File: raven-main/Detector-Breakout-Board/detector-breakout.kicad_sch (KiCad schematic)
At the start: 0 parts

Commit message: Added a power connector
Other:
- added sheet detector (detector.kicad_sch)
- added sheet power (power.kicad_sch)
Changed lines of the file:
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@@
 	(generator_version "10.0")
 	(paper "A4")
+	(sheet
+		(at 41.91 34.29)
+		(size 13.97 16.51)
+		(exclude_from_sim no)
+		(in_bom yes)
+		(on_board yes)
+		(dnp no)
+		(fields_autoplaced yes)
+		(stroke
+			(width 0.1524)
+			(type solid)
+		)
+		(fill
+			(color 0 0 0 0)
+		)
+		(property "Sheetname" "power"
+			(at 41.91 33.5784 0)
+			(show_name no)
+			(do_not_autoplace no)
+			(effects
+				(font
+					(size 1.27 1.27)
+				)
+				(justify left bottom)
+			)
+		)
+		(property "Sheetfile" "power.kicad_sch"
+			(at 41.91 51.3846 0)
+			(show_name no)
+			(do_not_autoplace no)
+			(effects
+				(font
+					(size 1.27 1.27)
+				)
+				(justify left top)
+			)
+		)
+		(instances
+			(project "detector-breakout"
+				(path "/88625785-cc97-4732-ad3f-8e674b21ece1"
+					(page "2")
+				)
+			)
+		)
+	)
+	(sheet
+		(at 77.47 34.29)
+		(size 15.24 16.51)
+		(exclude_from_sim no)
+		(in_bom yes)
+		(on_board yes)
+		(dnp no)
+		(fields_autoplaced yes)
+		(stroke
+			(width 0.1524)
+			(type solid)
+		)
+		(fill
+			(color 0 0 0 0)
+		)
+		(property "Sheetname" "detector"
+			(at 77.47 33.5784 0)
+			(show_name no)
+			(do_not_autoplace no)
+			(effects
+				(font
+					(size 1.27 1.27)
+				)
+				(justify left bottom)
+			)
+		)
+		(property "Sheetfile" "detector.kicad_sch"
+			(at 77.47 51.3846 0)
+			(show_name no)
+			(do_not_autoplace no)
+			(effects
+				(font
+					(size 1.27 1.27)
+				)
+				(justify left top)
+			)
+		)
+		(pin "Detector_Out_A" output
+			(at 92.71 36.83 0)
+			(effects
+				(font
+					(size 1.27 1.27)
+				)
+				(justify right)
+			)
+		)
+		(pin "Detector_Out_B" input
+			(at 92.71 39.37 0)
+			(effects
+				(font
+					(size 1.27 1.27)
+				)
+				(justify right)
+			)
+		)
+		(instances
+			(project "detector-breakout"
+				(path "/88625785-cc97-4732-ad3f-8e674b21ece1"
+					(page "3")
+				)
+			)
+		)
+	)
 	(sheet_instances
 		(path "/"

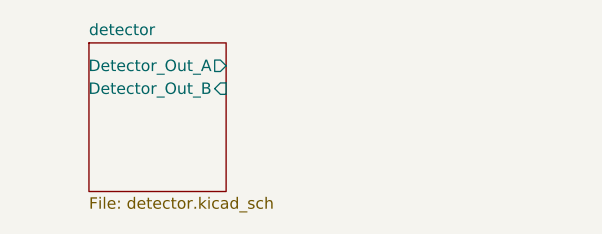
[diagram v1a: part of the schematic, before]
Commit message: Added power and output pins
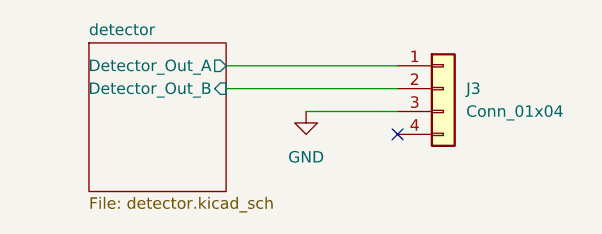
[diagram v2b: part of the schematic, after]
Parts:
- added J3: Conn_01x04, Connector_PinHeader_2.54mm:PinHeader_1x04_P2.54mm_Vertical, symbol Connector_Generic:Conn_01x04
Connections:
- net detector/Detector_Out_A: now also J3.1 (Pin_1)
- net detector/Detector_Out_B: now also J3.2 (Pin_2)
- new net GND: J3.3 (Pin_3)
- no-connect marks 0 -> 1
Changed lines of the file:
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@@
 	(generator_version "10.0")
 	(paper "A4")
+	(no_connect
+		(at 111.76 44.45)
+	)
+	(wire
+		(pts
+			(xy 92.71 39.37) (xy 111.76 39.37)
+		)
+		(stroke
+			(width 0)
+			(type default)
+		)
+	)
+	(wire
+		(pts
+			(xy 101.6 41.91) (xy 111.76 41.91)
+		)
+		(stroke
+			(width 0)
+			(type default)
+		)
+	)
+	(wire
+		(pts
+			(xy 92.71 36.83) (xy 111.76 36.83)
+		)
+		(stroke
+			(width 0)
+			(type default)
+		)
+	)
+	(symbol
+		(lib_id "power:GND")
+		(at 101.6 41.91 0)
+		(unit 1)
+		(body_style 1)
+		(exclude_from_sim no)
+		(in_bom yes)
+		(on_board yes)
+		(in_pos_files yes)
+		(dnp no)
+		(fields_autoplaced yes)
+		(property "Reference" "#PWR03"
+			(at 101.6 48.26 0)
+			(hide yes)
+			(show_name no)
+			(do_not_autoplace no)
+			(effects
+				(font
+					(size 1.27 1.27)
+				)
+			)
+		)
+		(property "Value" "GND"
+			(at 101.6 46.99 0)
+			(show_name no)
+			(do_not_autoplace no)
+			(effects
+				(font
+					(size 1.27 1.27)
+				)
+			)
+		)
+		(property "Footprint" ""
+			(at 101.6 41.91 0)
+			(hide yes)
+			(show_name no)
+			(do_not_autoplace no)
+			(effects
+				(font
+					(size 1.27 1.27)
+				)
+			)
+		)
+		(property "Datasheet" ""
+			(at 101.6 41.91 0)
+			(hide yes)
+			(show_name no)
+			(do_not_autoplace no)
+			(effects
+				(font
+					(size 1.27 1.27)
+				)
+			)
+		)
+		(property "Description" "Power symbol creates a global label with name \"GND\" , ground"
+			(at 101.6 41.91 0)
+			(hide yes)
+			(show_name no)
+			(do_not_autoplace no)
+			(effects
+				(font
+					(size 1.27 1.27)
+				)
+			)
+		)
+		(pin "1"
+		)
+		(instances
+			(project "detector-breakout"
+				(path "/88625785-cc97-4732-ad3f-8e674b21ece1"
+					(reference "#PWR03")
+					(unit 1)
+				)
+			)
+		)
+	)
+	(symbol
+		(lib_id "Connector_Generic:Conn_01x04")
+		(at 116.84 39.37 0)
+		(unit 1)
+		(body_style 1)
+		(exclude_from_sim no)
+		(in_bom yes)
+		(on_board yes)
+		(in_pos_files yes)
+		(dnp no)
+		(fields_autoplaced yes)
+		(property "Reference" "J3"
+			(at 119.38 39.3699 0)
+			(show_name no)
+			(do_not_autoplace no)
+			(effects
+				(font
+					(size 1.27 1.27)
+				)
+				(justify left)
+			)
+		)
+		(property "Value" "Conn_01x04"
+			(at 119.38 41.9099 0)
+			(show_name no)
+			(do_not_autoplace no)
+			(effects
+				(font
+					(size 1.27 1.27)
+				)
+				(justify left)
+			)
+		)
+		(property "Footprint" "Connector_PinHeader_2.54mm:PinHeader_1x04_P2.54mm_Vertical"
+			(at 116.84 39.37 0)
+			(hide yes)
+			(show_name no)
+			(do_not_autoplace no)
+			(effects
+				(font
+					(size 1.27 1.27)
+				)
+			)
+		)
+		(property "Datasheet" ""
+			(at 116.84 39.37 0)
+			(hide yes)
+			(show_name no)
+			(do_not_autoplace no)
+			(effects
+				(font
+					(size 1.27 1.27)
+				)
+			)
+		)
+		(property "Description" "Generic connector, single row, 01x04, script generated (kicad-library-utils/schlib/autogen/connector/)"
+			(at 116.84 39.37 0)
+			(hide yes)
+			(show_name no)
+			(do_not_autoplace no)
+			(effects
+				(font
+					(size 1.27 1.27)
+				)
+			)
+		)
+		(pin "3"
+		)
+		(pin "1"
+		)
+		(pin "2"
+		)
+		(pin "4"
+		)
+		(instances
+			(project "detector-breakout"
+				(path "/88625785-cc97-4732-ad3f-8e674b21ece1"
+					(reference "J3")
+					(unit 1)
+				)
+			)
+		)
+	)
 	(sheet
 		(at 41.91 34.29)

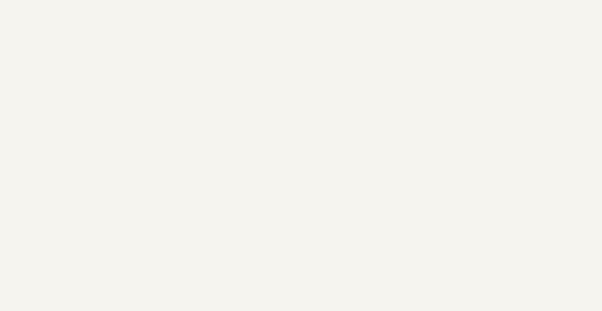
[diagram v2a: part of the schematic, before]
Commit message: Updated pcb layout
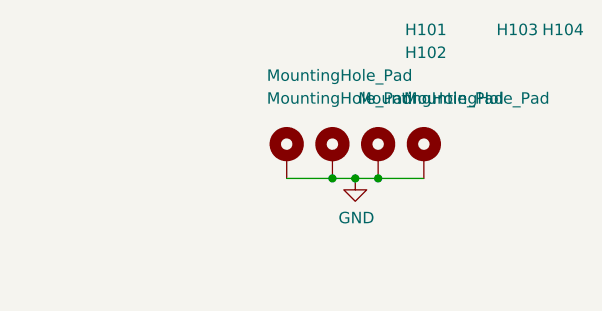
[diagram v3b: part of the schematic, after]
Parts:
- added H101, H102, H103, H104: MountingHole_Pad, MountingHole:MountingHole_3.2mm_M3_DIN965_Pad, symbol Mechanical:MountingHole_Pad
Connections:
- net GND: now also H101.1, H102.1, H103.1, H104.1
